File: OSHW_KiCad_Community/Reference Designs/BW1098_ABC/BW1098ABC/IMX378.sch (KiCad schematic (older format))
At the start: 11 parts

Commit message: skeleton complete, most footprints assigned, still need to check the transferred ones for dims
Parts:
- C? (x3): footprint (none) -> Capacitor_SMD:C_01005_0402Metric
- C? (x3): footprint (none) -> Capacitor_SMD:C_0201_0603Metric
- R?: footprint (none) -> Resistor_SMD:R_0402_1005Metric
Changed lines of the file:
@@
 $Descr A4 11693 8268
 encoding utf-8
-Sheet 3 5
+Sheet 3 6
 Title ""
 Date ""
@@
 F 0 "C?" V 6110 5610 60  0000 R TNN
 F 1 "0.1uF 0402" V 6010 5610 60  0000 R TNN
-F 2 "" H 6010 5610 60  0001 C CNN
+F 2 "Capacitor_SMD:C_01005_0402Metric" H 6010 5610 60  0001 C CNN
 F 3 "" H 6010 5610 60  0000 C CNN
 F 4 "10V" V -1300 500 60  0001 C CNN "Voltage Rating"
@@
 F 0 "C?" V 5410 5610 60  0000 R TNN
 F 1 "10uF 0603" V 5310 5610 60  0000 R TNN
-F 2 "" H 5310 5610 60  0001 C CNN
+F 2 "Capacitor_SMD:C_0201_0603Metric" H 5310 5610 60  0001 C CNN
 F 3 "" H 5310 5610 60  0000 C CNN
 F 4 "10V" V -1300 500 60  0000 C CNN "Voltage Rating"
@@
 F 0 "C?" V 6710 5610 60  0000 R TNN
 F 1 "10uF 0603" V 6610 5610 60  0000 R TNN
-F 2 "" H 6610 5610 60  0001 C CNN
+F 2 "Capacitor_SMD:C_0201_0603Metric" H 6610 5610 60  0001 C CNN
 F 3 "" H 6610 5610 60  0000 C CNN
 F 4 "10V" V -1300 500 60  0001 C CNN "Voltage Rating"
@@
 F 0 "C?" V 7410 5610 60  0000 R TNN
 F 1 "0.1uF 0402" V 7310 5610 60  0000 R TNN
-F 2 "" H 7310 5610 60  0001 C CNN
+F 2 "Capacitor_SMD:C_01005_0402Metric" H 7310 5610 60  0001 C CNN
 F 3 "" H 7310 5610 60  0000 C CNN
 F 4 "10V" V -1300 500 60  0001 C CNN "Voltage Rating"
@@
 F 0 "C?" V 8010 5610 60  0000 R TNN
 F 1 "10uF 0603" V 7910 5610 60  0000 R TNN
-F 2 "" H 7910 5610 60  0001 C CNN
+F 2 "Capacitor_SMD:C_0201_0603Metric" H 7910 5610 60  0001 C CNN
 F 3 "" H 7910 5610 60  0000 C CNN
 F 4 "10V" V -1300 500 60  0001 C CNN "Voltage Rating"
@@
 F 0 "R?" H 8390 3730 60  0000 L BNN
 F 1 "10K 0402" H 8390 3570 60  0000 L BNN
-F 2 "" H 8390 3570 60  0001 C CNN
+F 2 "Resistor_SMD:R_0402_1005Metric" H 8390 3570 60  0001 C CNN
 F 3 "" H 8390 3570 60  0000 C CNN
 	1    8300 3700
@@
 F 0 "C?" V 4810 5610 60  0000 R TNN
 F 1 "0.1uF 0402" V 4710 5610 60  0000 R TNN
-F 2 "" H 4710 5610 60  0001 C CNN
+F 2 "Capacitor_SMD:C_01005_0402Metric" H 4710 5610 60  0001 C CNN
 F 3 "" H 4710 5610 60  0001 C CNN
 F 4 "10V" V -1300 500 60  0000 C CNN "Voltage Rating"

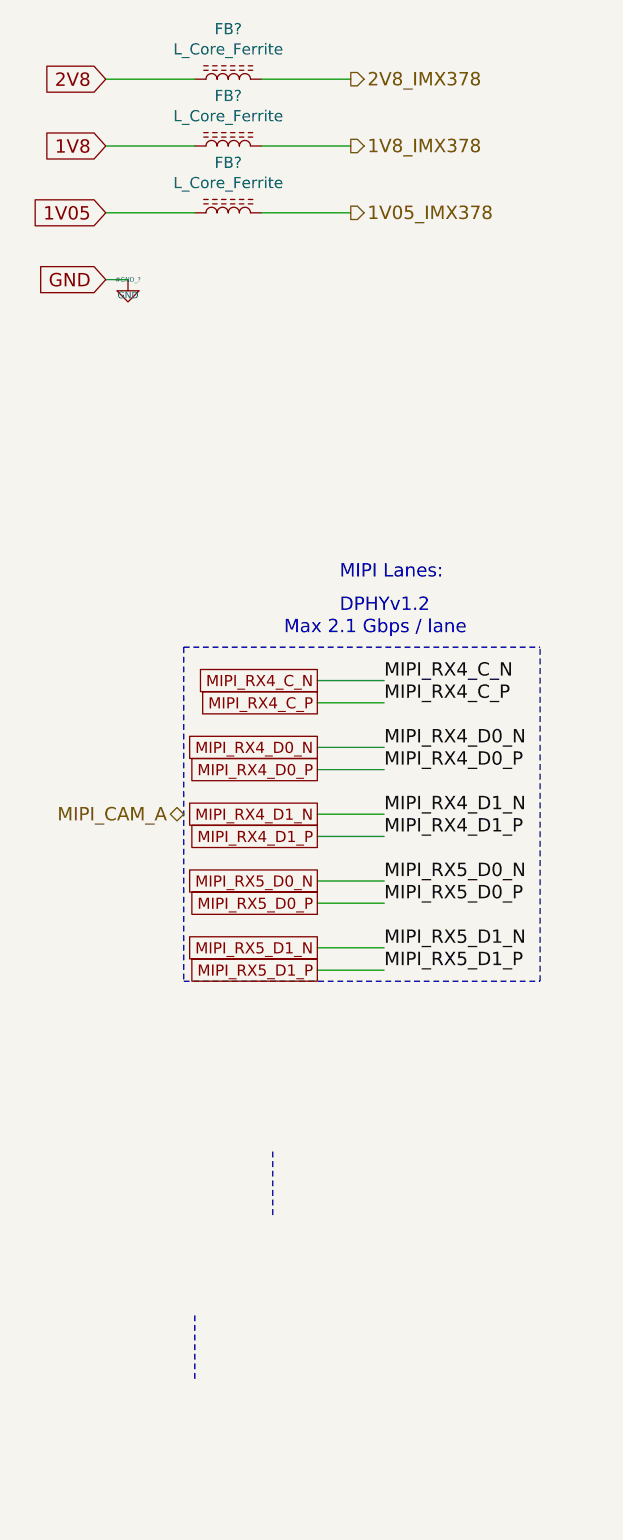
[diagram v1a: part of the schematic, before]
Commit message: schematic edits for BW1098ABC
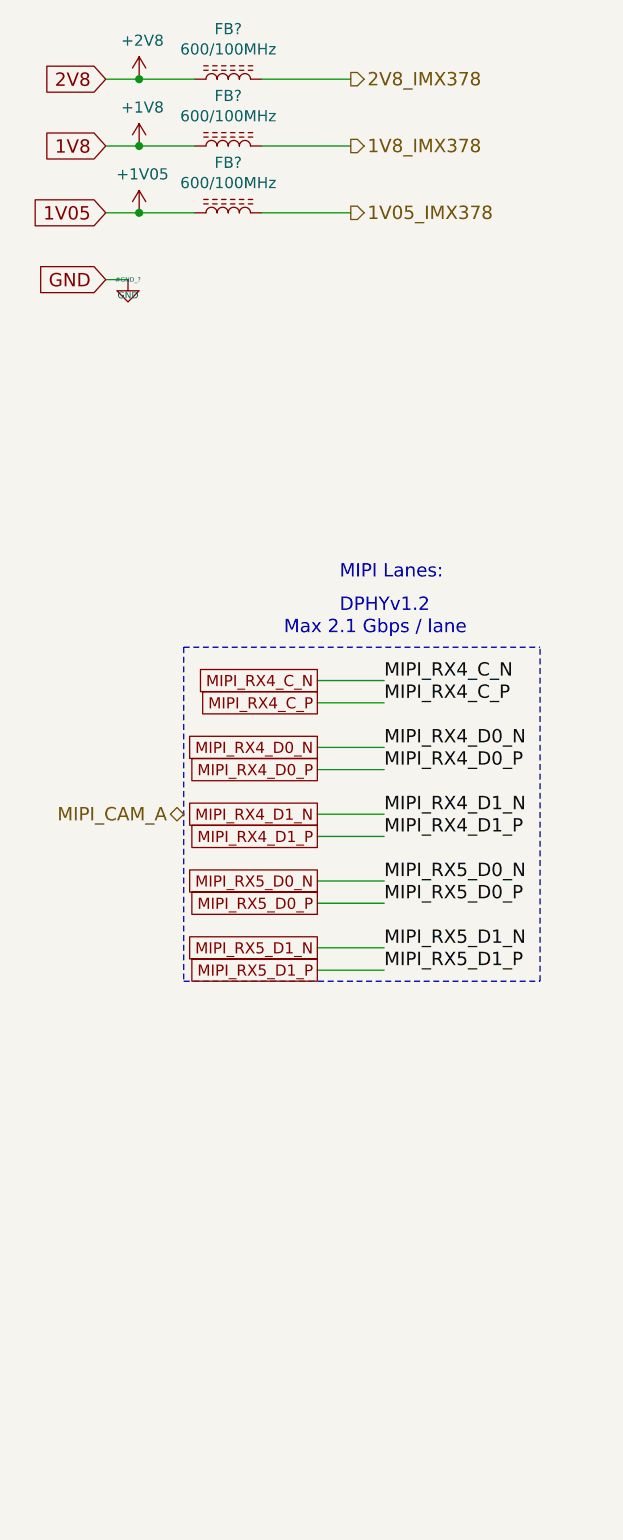
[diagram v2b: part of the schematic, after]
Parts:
- removed FB? (x2): L_Core_Ferrite, Ferrite_THT:LairdTech_28C0236-0JW-10, symbol Device:L_Core_Ferrite
- added FB? (x2): 600/100MHz, Ferrite_THT:LairdTech_28C0236-0JW-10, symbol Device:L_Core_Ferrite
- FB?: value L_Core_Ferrite -> 600/100MHz
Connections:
- net labels added: +1V05, +1V8, +2V8
- wire segments 70 -> 73
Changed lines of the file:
@@
 	1050 1700 950  1700
 Wire Wire Line
-	2050 1100 1650 1100
-Wire Wire Line
-	2050 800  1650 800
-Wire Wire Line
-	2050 1400 1650 1400
-Wire Notes Line
-	1350 6350 1350 6650
-Wire Notes Line
-	1700 5900 1700 5600
-Wire Wire Line
-	950  800  1350 800
-Wire Wire Line
-	950  1100 1350 1100
-Wire Wire Line
-	950  1400 1350 1400
+	950  800  1100 800
+Wire Wire Line
+	950  1100 1100 1100
+Wire Wire Line
+	950  1400 1100 1400
 Text HLabel 2050 800  2    60   Output ~ 0
 2V8_IMX378
@@
 P 1500 800
 F 0 "FB?" V 1725 800 50  0000 C CNN
-F 1 "L_Core_Ferrite" V 1634 800 50  0000 C CNN
+F 1 "600/100MHz" V 1634 800 50  0000 C CNN
 F 2 "Ferrite_THT:LairdTech_28C0236-0JW-10" H 1500 800 50  0001 C CNN
 F 3 "~" H 1500 800 50  0001 C CNN
 	1    1500 800
-	0    -1   -1   0
-$EndComp
-$Comp
-L Device:L_Core_Ferrite FB?
-U 1 1 5FFDA5E7
-P 1500 1100
-F 0 "FB?" V 1725 1100 50  0000 C CNN
-F 1 "L_Core_Ferrite" V 1634 1100 50  0000 C CNN
-F 2 "Ferrite_THT:LairdTech_28C0236-0JW-10" H 1500 1100 50  0001 C CNN
-F 3 "~" H 1500 1100 50  0001 C CNN
-	1    1500 1100
-	0    -1   -1   0
-$EndComp
-$Comp
-L Device:L_Core_Ferrite FB?
-U 1 1 5FFDAE40
-P 1500 1400
-F 0 "FB?" V 1725 1400 50  0000 C CNN
-F 1 "L_Core_Ferrite" V 1634 1400 50  0000 C CNN
-F 2 "Ferrite_THT:LairdTech_28C0236-0JW-10" H 1500 1400 50  0001 C CNN
-F 3 "~" H 1500 1400 50  0001 C CNN
-	1    1500 1400
 	0    -1   -1   0
 $EndComp
@@
 Wire Wire Line
 	8300 2750 7400 2750
+$Comp
+L power:+1V8 #PWR?
+U 1 1 5FFCE432
+P 1100 1100
+AR Path="/604AEAFA/5FFCE432" Ref="#PWR?"  Part="1"
+AR Path="/5FF8D4A5/5FFCE432" Ref="#PWR?"  Part="1"
+F 0 "#PWR?" H 1100 950 50  0001 C CNN
+F 1 "+1V8" H 1115 1273 50  0000 C CNN
+F 2 "" H 1100 1100 50  0001 C CNN
+F 3 "" H 1100 1100 50  0001 C CNN
+	1    1100 1100
+	1    0    0    -1
+$EndComp
+$Comp
+L power:+2V8 #PWR?
+U 1 1 5FFCE438
+P 1100 800
+AR Path="/604AEAFA/5FFCE438" Ref="#PWR?"  Part="1"
+AR Path="/5FF8D4A5/5FFCE438" Ref="#PWR?"  Part="1"
+F 0 "#PWR?" H 1100 650 50  0001 C CNN
+F 1 "+2V8" H 1115 973 50  0000 C CNN
+F 2 "" H 1100 800 50  0001 C CNN
+F 3 "" H 1100 800 50  0001 C CNN
+	1    1100 800
+	1    0    0    -1
+$EndComp
+$Comp
+L depthAI_sch:+1V05 #PWR?
+U 1 1 5FFCE43E
+P 1100 1400
+AR Path="/604AEAFA/5FFCE43E" Ref="#PWR?"  Part="1"
+AR Path="/5FF8D4A5/5FFCE43E" Ref="#PWR?"  Part="1"
+F 0 "#PWR?" H 1100 1250 50  0001 C CNN
+F 1 "+1V05" H 1115 1573 50  0000 C CNN
+F 2 "" H 1100 1400 50  0001 C CNN
+F 3 "" H 1100 1400 50  0001 C CNN
+	1    1100 1400
+	1    0    0    -1
+$EndComp
+Connection ~ 1100 1400
+Wire Wire Line
+	1100 1400 1350 1400
+Wire Wire Line
+	1650 1400 2050 1400
+Connection ~ 1100 1100
+Wire Wire Line
+	1100 1100 1350 1100
+Wire Wire Line
+	1650 1100 2050 1100
+Connection ~ 1100 800
+Wire Wire Line
+	1100 800  1350 800
+Wire Wire Line
+	1650 800  2050 800
+$Comp
+L Device:L_Core_Ferrite FB?
+U 1 1 5FFE6B4A
+P 1500 1100
+F 0 "FB?" V 1725 1100 50  0000 C CNN
+F 1 "600/100MHz" V 1634 1100 50  0000 C CNN
+F 2 "Ferrite_THT:LairdTech_28C0236-0JW-10" H 1500 1100 50  0001 C CNN
+F 3 "~" H 1500 1100 50  0001 C CNN
+	1    1500 1100
+	0    -1   -1   0
+$EndComp
+$Comp
+L Device:L_Core_Ferrite FB?
+U 1 1 5FFE73DF
+P 1500 1400
+F 0 "FB?" V 1725 1400 50  0000 C CNN
+F 1 "600/100MHz" V 1634 1400 50  0000 C CNN
+F 2 "Ferrite_THT:LairdTech_28C0236-0JW-10" H 1500 1400 50  0001 C CNN
+F 3 "~" H 1500 1400 50  0001 C CNN
+	1    1500 1400
+	0    -1   -1   0
+$EndComp
 $EndSCHEMATC

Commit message: small stuff
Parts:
- C? (x3): symbol depthAI_sch:GRM155R71A104JA01D -> BW1098ABC-rescue:GRM155R71A104JA01D-depthAI_sch
- C? (x3): symbol depthAI_sch:GRM188R61A106ME69D -> BW1098ABC-rescue:GRM188R61A106ME69D-depthAI_sch
- J?: symbol depthAI_sch:A12N02A-201 -> BW1098ABC-rescue:A12N02A-201-depthAI_sch
- R?: symbol depthAI_sch:RC0402FR-1310KL -> BW1098ABC-rescue:RC0402FR-1310KL-depthAI_sch
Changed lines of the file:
@@
 	4000 1900 4000 2500
 $Comp
-L depthAI_sch:GRM155R71A104JA01D C?
+L BW1098ABC-rescue:GRM155R71A104JA01D-depthAI_sch C?
 U 1 1 5FFB0B02
 P 6000 5700
@@
 $EndComp
 $Comp
-L depthAI_sch:GRM188R61A106ME69D C?
+L BW1098ABC-rescue:GRM188R61A106ME69D-depthAI_sch C?
 U 1 1 5FFB0AFB
 P 5300 5700
@@
 $EndComp
 $Comp
-L depthAI_sch:GRM188R61A106ME69D C?
+L BW1098ABC-rescue:GRM188R61A106ME69D-depthAI_sch C?
 U 1 1 5FFB0AF4
 P 6600 5700
@@
 $EndComp
 $Comp
-L depthAI_sch:GRM155R71A104JA01D C?
+L BW1098ABC-rescue:GRM155R71A104JA01D-depthAI_sch C?
 U 1 1 5FFB0AED
 P 7300 5700
@@
 $EndComp
 $Comp
-L depthAI_sch:GRM188R61A106ME69D C?
+L BW1098ABC-rescue:GRM188R61A106ME69D-depthAI_sch C?
 U 1 1 5FFB0AE6
 P 7900 5700
@@
 $EndComp
 $Comp
-L depthAI_sch:RC0402FR-1310KL R?
+L BW1098ABC-rescue:RC0402FR-1310KL-depthAI_sch R?
 U 1 1 5FFB0ADF
 P 8300 3700
@@
 $EndComp
 $Comp
-L depthAI_sch:A12N02A-201 J?
+L BW1098ABC-rescue:A12N02A-201-depthAI_sch J?
 U 1 1 5FFB0ACD
 P 5300 4500
@@
 $EndComp
 $Comp
-L depthAI_sch:GRM155R71A104JA01D C?
+L BW1098ABC-rescue:GRM155R71A104JA01D-depthAI_sch C?
 U 1 1 5FFB0AC7
 P 4700 5700
@@
 $EndComp
 $Comp
-L depthAI_sch:+1V05 #PWR?
+L BW1098ABC-rescue:+1V05-depthAI_sch #PWR?
 U 1 1 5FFCE43E
 P 1100 1400

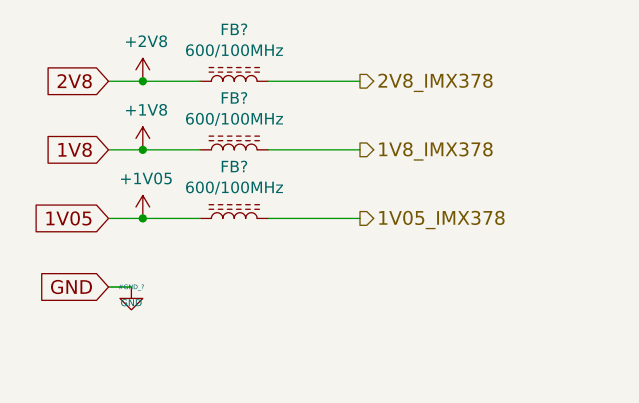
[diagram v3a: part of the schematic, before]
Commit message: all footprints associated on bw1098abc board except two I need to clarify with Brian. Need to talk to chris about power
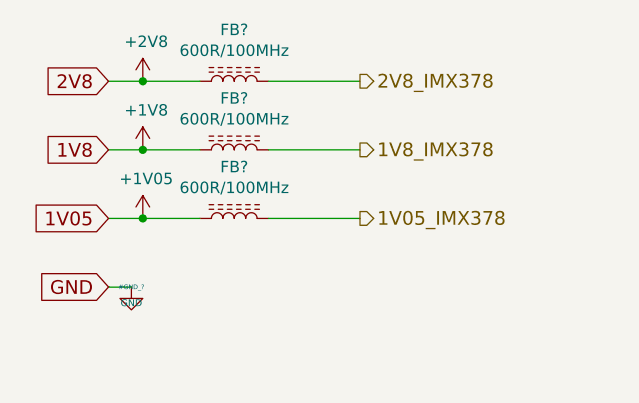
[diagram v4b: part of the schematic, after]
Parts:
- C? (x3): footprint Capacitor_SMD:C_01005_0402Metric -> Capacitor_SMD:C_0402_1005Metric
- C? (x3): footprint Capacitor_SMD:C_0201_0603Metric -> Capacitor_SMD:C_0603_1608Metric
- FB? (x3): value 600/100MHz -> 600R/100MHz; footprint Ferrite_THT:LairdTech_28C0236-0JW-10 -> OSHW_LuxonisMaster_20201223:2508056017Y2
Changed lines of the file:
@@
 P 1500 800
 F 0 "FB?" V 1725 800 50  0000 C CNN
-F 1 "600/100MHz" V 1634 800 50  0000 C CNN
-F 2 "Ferrite_THT:LairdTech_28C0236-0JW-10" H 1500 800 50  0001 C CNN
+F 1 "600R/100MHz" V 1634 800 50  0000 C CNN
+F 2 "OSHW_LuxonisMaster_20201223:2508056017Y2" H 1500 800 50  0001 C CNN
 F 3 "~" H 1500 800 50  0001 C CNN
 	1    1500 800
@@
 F 0 "C?" V 6110 5610 60  0000 R TNN
 F 1 "0.1uF 0402" V 6010 5610 60  0000 R TNN
-F 2 "Capacitor_SMD:C_01005_0402Metric" H 6010 5610 60  0001 C CNN
+F 2 "Capacitor_SMD:C_0402_1005Metric" H 6010 5610 60  0001 C CNN
 F 3 "" H 6010 5610 60  0000 C CNN
 F 4 "10V" V -1300 500 60  0001 C CNN "Voltage Rating"
@@
 F 0 "C?" V 5410 5610 60  0000 R TNN
 F 1 "10uF 0603" V 5310 5610 60  0000 R TNN
-F 2 "Capacitor_SMD:C_0201_0603Metric" H 5310 5610 60  0001 C CNN
+F 2 "Capacitor_SMD:C_0603_1608Metric" H 5310 5610 60  0001 C CNN
 F 3 "" H 5310 5610 60  0000 C CNN
 F 4 "10V" V -1300 500 60  0000 C CNN "Voltage Rating"
@@
 F 0 "C?" V 6710 5610 60  0000 R TNN
 F 1 "10uF 0603" V 6610 5610 60  0000 R TNN
-F 2 "Capacitor_SMD:C_0201_0603Metric" H 6610 5610 60  0001 C CNN
+F 2 "Capacitor_SMD:C_0603_1608Metric" H 6610 5610 60  0001 C CNN
 F 3 "" H 6610 5610 60  0000 C CNN
 F 4 "10V" V -1300 500 60  0001 C CNN "Voltage Rating"
@@
 F 0 "C?" V 7410 5610 60  0000 R TNN
 F 1 "0.1uF 0402" V 7310 5610 60  0000 R TNN
-F 2 "Capacitor_SMD:C_01005_0402Metric" H 7310 5610 60  0001 C CNN
+F 2 "Capacitor_SMD:C_0402_1005Metric" H 7310 5610 60  0001 C CNN
 F 3 "" H 7310 5610 60  0000 C CNN
 F 4 "10V" V -1300 500 60  0001 C CNN "Voltage Rating"
@@
 F 0 "C?" V 8010 5610 60  0000 R TNN
 F 1 "10uF 0603" V 7910 5610 60  0000 R TNN
-F 2 "Capacitor_SMD:C_0201_0603Metric" H 7910 5610 60  0001 C CNN
+F 2 "Capacitor_SMD:C_0603_1608Metric" H 7910 5610 60  0001 C CNN
 F 3 "" H 7910 5610 60  0000 C CNN
 F 4 "10V" V -1300 500 60  0001 C CNN "Voltage Rating"
@@
 F 0 "C?" V 4810 5610 60  0000 R TNN
 F 1 "0.1uF 0402" V 4710 5610 60  0000 R TNN
-F 2 "Capacitor_SMD:C_01005_0402Metric" H 4710 5610 60  0001 C CNN
+F 2 "Capacitor_SMD:C_0402_1005Metric" H 4710 5610 60  0001 C CNN
 F 3 "" H 4710 5610 60  0001 C CNN
 F 4 "10V" V -1300 500 60  0000 C CNN "Voltage Rating"
@@
 P 1500 1100
 F 0 "FB?" V 1725 1100 50  0000 C CNN
-F 1 "600/100MHz" V 1634 1100 50  0000 C CNN
-F 2 "Ferrite_THT:LairdTech_28C0236-0JW-10" H 1500 1100 50  0001 C CNN
+F 1 "600R/100MHz" V 1634 1100 50  0000 C CNN
+F 2 "OSHW_LuxonisMaster_20201223:2508056017Y2" H 1500 1100 50  0001 C CNN
 F 3 "~" H 1500 1100 50  0001 C CNN
 	1    1500 1100
@@
 P 1500 1400
 F 0 "FB?" V 1725 1400 50  0000 C CNN
-F 1 "600/100MHz" V 1634 1400 50  0000 C CNN
-F 2 "Ferrite_THT:LairdTech_28C0236-0JW-10" H 1500 1400 50  0001 C CNN
+F 1 "600R/100MHz" V 1634 1400 50  0000 C CNN
+F 2 "OSHW_LuxonisMaster_20201223:2508056017Y2" H 1500 1400 50  0001 C CNN
 F 3 "~" H 1500 1400 50  0001 C CNN
 	1    1500 1400
